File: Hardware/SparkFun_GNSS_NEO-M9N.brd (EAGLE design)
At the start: 64.9 x 38 mm, 74 parts, among them J1 MICROMOD_STANDARD, J4 Bus Selection, U1 U-BLOX_NEO-M9N, U2 3.3V, U3 EEPROM, U4 74HC1G04

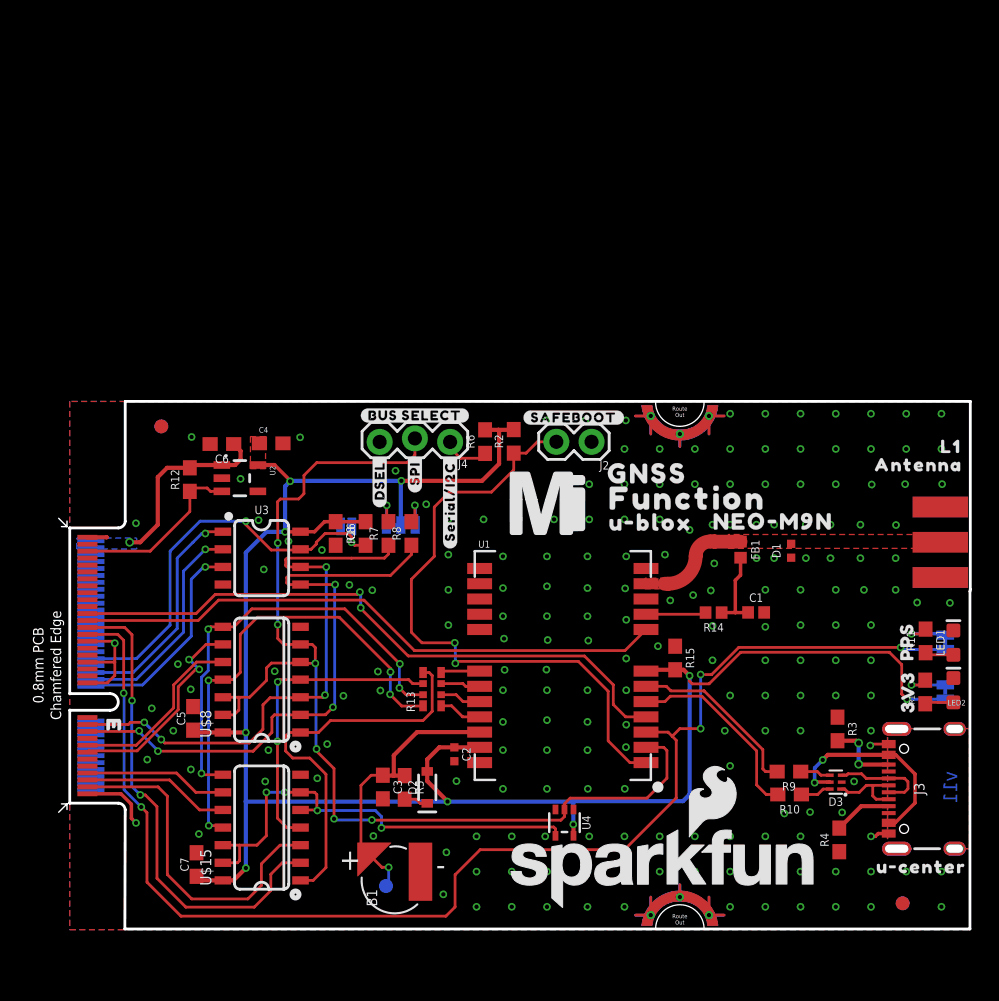
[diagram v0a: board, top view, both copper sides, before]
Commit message: Adds PTH selection silk to bottom
* Chnages MISO/MOSI net label -> PICO/POCI
* Adds text explanation to safeboot pth selection
* Moves some nets around for better ground pour
* Adds a few vias
* Adds measures to LEDs
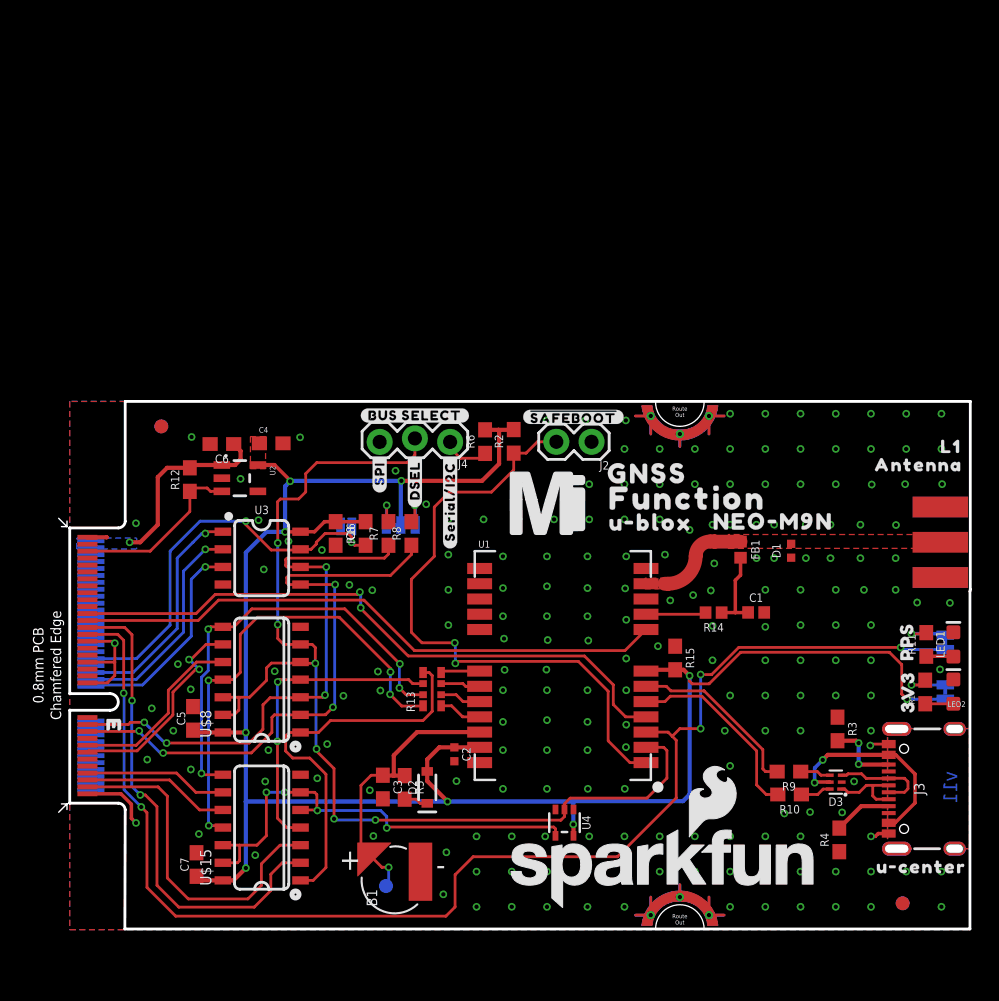
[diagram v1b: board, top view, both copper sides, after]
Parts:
- added U$22: (no value), top:#BUS_SELECT#509
- added U$23: (no value), neom9n:##SAFEBOOT##882188213
- added U$24: (no value), top:#SPI#40313521
- added U$25: (no value), top:#DSEL#40313522
- added U$26: (no value), top:#SERIAL#I2C#40313523
- U$4: device top:#SAFEBOOT#12 -> neom9n:##SAFEBOOT##882188213
- moved U$16 2.54 mm to (22.4, 32.9)
- moved U$19 2.54 mm to (24.9, 32.4)
- moved R11 0.26 mm to (61.8, 20.6)
- moved LED1 0.13 mm to (63.7, 20.6)
- moved LED2 0.10 mm to (63.7, 17.2)
- moved U$4 0.06 mm to (36.3, 37.0)
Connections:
- net RXI/SDI renamed RXI/PICO
- net SDI renamed PICO
- net SDO renamed POCI
- net TXO/SDO renamed TXO/POCI
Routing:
- net GND: vias 201 -> 204

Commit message: Replaces SMA connector with u.FL
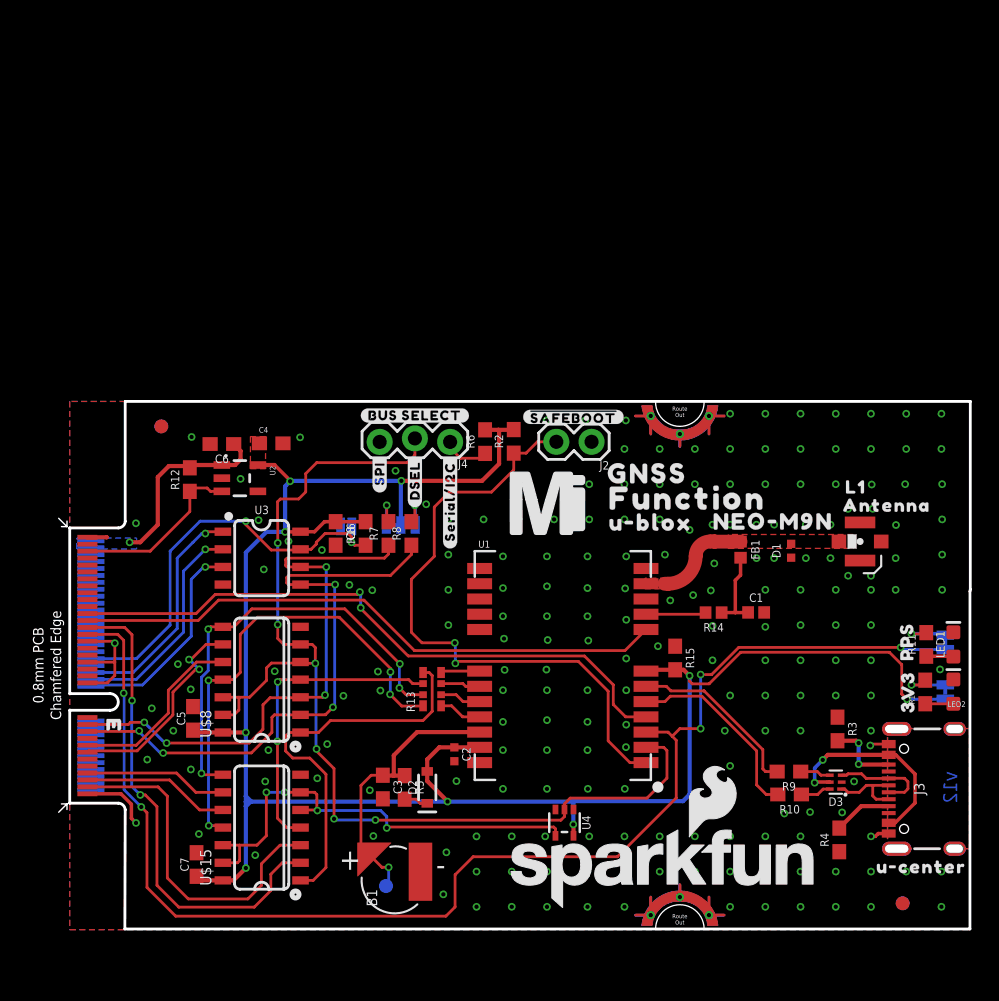
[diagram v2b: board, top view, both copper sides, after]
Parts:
- E1: value ANTENNA-SMA-GROUNDEDEDGE_SMA_THIN -> U.FL; device SparkFun-RF:SMA-EDGE -> SparkFun-Connectors:U.FL
- R5: value 1k -> 3.3k
- R7, R8: value 4.7k -> 2.2k
- moved U$14 7.45 mm to (56.7, 31.9)
- moved E1 5.79 mm to (57.0, 28.0), turned to 180 degrees
- moved U$7 3.71 mm to (58.9, 30.6)
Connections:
- net GND: now also E1.1, E1.2; no longer E1.GND@0, E1.GND@1, E1.GND@2, E1.GND@3
- net GPS_ANT1: now also E1.FEED; no longer E1.SIG
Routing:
- net 3.3V: track 147.1 -> 148.2 mm
- net GND: vias 204 -> 207
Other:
- board text added: "v12"
- board text removed: "v11"

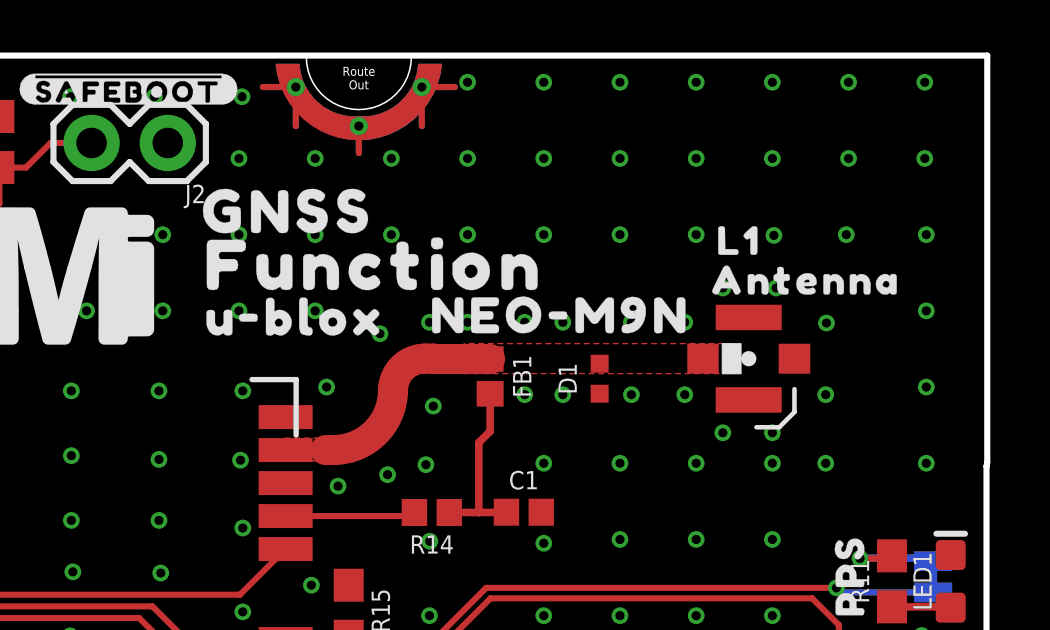
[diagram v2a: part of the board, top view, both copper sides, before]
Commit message: Replaces old ML414H reflowable with new MS421R
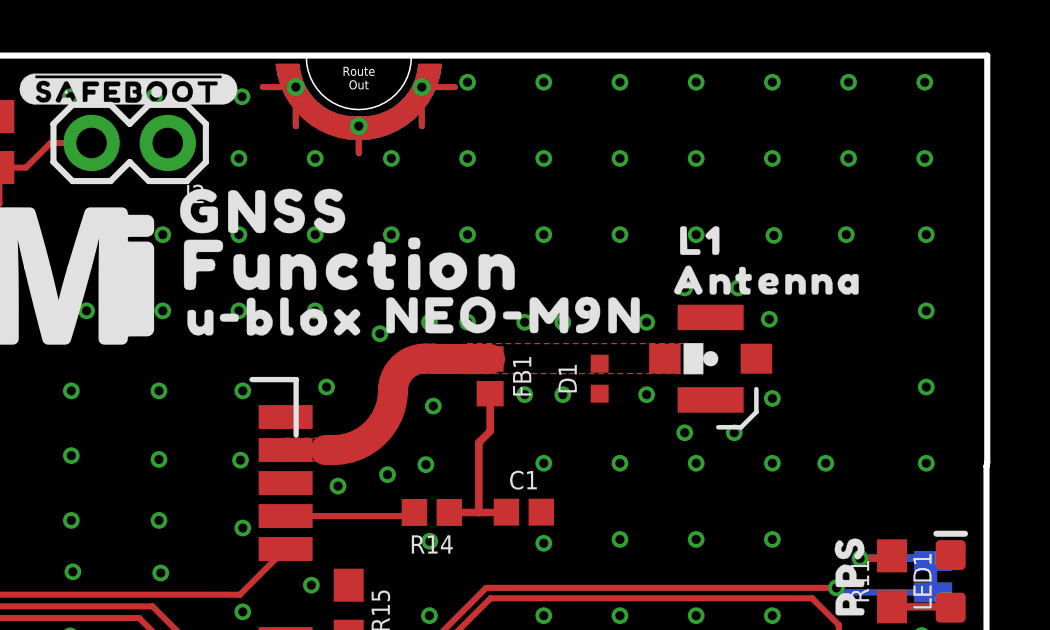
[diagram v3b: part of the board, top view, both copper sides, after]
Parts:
- B1: device SparkFun-Batteries:ML414H_IV01E -> SparkFun-Batteries:MS421R_IV03E
- moved U$6 1.52 mm to (49.2, 29.4)
- moved E1 1.27 mm to (55.7, 28.0)
- moved U$14 1.27 mm to (55.4, 31.9)
- moved U$7 1.27 mm to (57.7, 30.6)
- moved U$21 0.76 mm to (40.9, 32.9)
- moved U$3 0.76 mm to (43.8, 31.1)
- moved U$5 0.63 mm to (41.2, 29.4)
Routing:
- net GND: vias 207 -> 205
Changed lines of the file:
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@@
 <attribute name="VALUE" x="22.7076" y="12.9554" size="0.6096" layer="27" font="vector" ratio="20" rot="R270" align="top-center"/>
 </element>
-<element name="B1" library="SparkFun-Batteries" package="ML414H_IV01E" value="6.8MM_COIN_CELL" x="23.4442" y="3.5814" smashed="yes" rot="R90">
+<element name="B1" library="SparkFun-Batteries" package="MS421R_IV03E" value="6.8MM_COIN_CELL" x="23.4442" y="3.5814" smashed="yes" rot="R90">
 <attribute name="NAME" x="22.174196875" y="1.676396875" size="0.762" layer="25" ratio="15" rot="R90"/>
-<attribute name="PROD_ID" value="BATT-14267" x="23.4442" y="3.5814" size="1.778" layer="27" rot="R90" display="off"/>
+<attribute name="PROD_ID" value="BAT-16685" x="23.4442" y="3.5814" size="1.778" layer="27" rot="R90" display="off"/>
 </element>
 <element name="R7" library="SparkFun-Resistors" package="0603" value="2.2k" x="22.987" y="28.575" smashed="yes" rot="R90">
@@
 <attribute name="VALUE" x="62.5348" y="10.16" size="0.762" layer="27" rot="R90" align="center"/>
 </element>
-<element name="E1" library="SparkFun-Connectors" package="U.FL" value="U.FL" x="56.9976" y="27.9962" smashed="yes" rot="R180">
-<attribute name="PROD_ID" value="CONN-09193" x="56.9976" y="27.9962" size="1.778" layer="27" rot="R180" display="off"/>
-<attribute name="SF_ID" value="WRL-09144" x="56.9976" y="27.9962" size="1.778" layer="27" rot="R180" display="off"/>
-<attribute name="VALUE" value="U.FL" x="56.9976" y="27.9962" size="1.778" layer="27" rot="R180" display="off"/>
+<element name="E1" library="SparkFun-Connectors" package="U.FL" value="U.FL" x="55.7276" y="27.9962" smashed="yes" rot="R180">
+<attribute name="PROD_ID" value="CONN-09193" x="55.7276" y="27.9962" size="1.778" layer="27" rot="R180" display="off"/>
+<attribute name="SF_ID" value="WRL-09144" x="55.7276" y="27.9962" size="1.778" layer="27" rot="R180" display="off"/>
+<attribute name="VALUE" value="U.FL" x="55.7276" y="27.9962" size="1.778" layer="27" rot="R180" display="off"/>
 </element>
 <element name="FB1" library="SparkFun-Coils" package="0402" value="120Ω" x="48.3774" y="27.4064" smashed="yes" rot="R270">
@@
 <element name="U$1" library="top" package="3V313" value="" x="60.452" y="17.145" smashed="yes" rot="R90"/>
 <element name="U$2" library="top" package="PPS13" value="" x="60.3758" y="20.7772" smashed="yes" rot="R90"/>
-<element name="U$5" library="top" package="U#BLOX11" value="" x="41.8846" y="29.3624" smashed="yes"/>
-<element name="U$6" library="top" package="NEO#M9N12" value="" x="50.7238" y="29.4386" smashed="yes"/>
-<element name="U$7" library="top" package="ANTENNA14" value="" x="58.928" y="30.607" smashed="yes"/>
+<element name="U$5" library="top" package="U#BLOX11" value="" x="41.2496" y="29.3624" smashed="yes"/>
+<element name="U$6" library="top" package="NEO#M9N12" value="" x="49.1998" y="29.4386" smashed="yes"/>
+<element name="U$7" library="top" package="ANTENNA14" value="" x="57.658" y="30.607" smashed="yes"/>
 <element name="U$9" library="top" package="U#CENTER15" value="" x="61.41" y="4.538" smashed="yes"/>
 <element name="U$10" library="top" package="#I2C#18" value="" x="23.912" y="27.424" smashed="yes" rot="MR0"/>
@@
 <element name="LOGO2" library="SparkFun-Aesthetics" package="SFE_LOGO_NAME_FLAME_.2" value="SFE_LOGO_NAME_FLAME.2_INCH" x="42.799" y="4.4196" smashed="yes"/>
 <element name="LOGO3" library="SparkFun-Aesthetics" package="OSHW-LOGO-S" value="OSHW-LOGOS" x="10.16" y="2.54" smashed="yes" rot="MR0"/>
-<element name="U$3" library="top" package="FUNCTION521" value="" x="44.5262" y="31.115" smashed="yes"/>
+<element name="U$3" library="top" package="FUNCTION521" value="" x="43.7642" y="31.115" smashed="yes"/>
 <element name="R3" library="SparkFun-Resistors" package="0603" value="5.1k" x="55.372" y="14.478" smashed="yes" rot="R270">
 <attribute name="NAME" x="56.134" y="14.478" size="0.6096" layer="25" font="vector" ratio="20" rot="R270" align="bottom-center"/>
@@
 </element>
 <element name="U$11" library="SparkFun-MicroMod" package="MICROMOD_MI_LOGO_1" value="" x="34.4932" y="30.7848" smashed="yes"/>
-<element name="U$14" library="top" package="L1321542" value="" x="56.6928" y="31.9278" smashed="yes"/>
+<element name="U$14" library="top" package="L1321542" value="" x="55.4228" y="31.9278" smashed="yes"/>
 <element name="U$8" library="SparkFun-IC-Logic" package="SO14" value="74LVC4066D_QUAD_BILATERAL_SWITCH" x="13.843" y="17.399" smashed="yes" rot="R90">
 <attribute name="NAME" x="10.2108" y="13.843" size="0.8128" layer="25" font="vector" ratio="16" rot="R90"/>
@@
 </element>
 <element name="U$20" library="top" package="#WP#13215403132222564" value="" x="19.812" y="27.432" smashed="yes" rot="MR0"/>
-<element name="U$21" library="top" package="GNSS2222502" value="" x="41.656" y="32.893" smashed="yes"/>
+<element name="U$21" library="top" package="GNSS2222502" value="" x="40.894" y="32.893" smashed="yes"/>
 <element name="U$12" library="top" package="#3V3_LED#403132222514" value="" x="59.563" y="17.145" smashed="yes" rot="MR0"/>
 <element name="U$13" library="top" package="#PPS_LED#403132222514" value="" x="59.563" y="20.701" smashed="yes" rot="MR0"/>
@@
 <wire x1="43.2" y1="35.75" x2="41.9" y2="37.05" width="0.2032" layer="1"/>
 <via x="60.2488" y="32.131" extent="1-16" drill="0.3048"/>
-<via x="59.5884" y="29.1846" extent="1-16" drill="0.3048"/>
+<via x="57.6834" y="29.3116" extent="1-16" drill="0.3048"/>
 <contactref element="R3" pad="1"/>
 <contactref element="R4" pad="1"/>
@@
 <via x="52.705" y="24.511" extent="1-16" drill="0.3048"/>
 <via x="55.245" y="24.511" extent="1-16" drill="0.3048"/>
-<via x="54.864" y="29.21" extent="1-16" drill="0.3048"/>
-<via x="53.086" y="29.21" extent="1-16" drill="0.3048"/>
+<via x="53.594" y="29.21" extent="1-16" drill="0.3048"/>
 <via x="44.704" y="28.829" extent="1-16" drill="0.3048"/>
 <via x="46.482" y="26.416" extent="1-16" drill="0.3048"/>
 <via x="43.307" y="23.749" extent="1-16" drill="0.3048"/>
 <via x="44.958" y="24.13" extent="1-16" drill="0.3048"/>
-<via x="57.912" y="30.353" extent="1-16" drill="0.3048"/>
+<via x="56.642" y="30.353" extent="1-16" drill="0.3048"/>
 <via x="57.785" y="24.511" extent="1-16" drill="0.3048"/>
-<via x="59.563" y="26.797" extent="1-16" drill="0.3048"/>
-<via x="57.785" y="25.527" extent="1-16" drill="0.3048"/>
-<via x="54.864" y="26.797" extent="1-16" drill="0.3048"/>
-<via x="53.086" y="26.797" extent="1-16" drill="0.3048"/>
+<via x="57.785" y="26.67" extent="1-16" drill="0.3048"/>
+<via x="56.515" y="25.527" extent="1-16" drill="0.3048"/>
+<via x="53.594" y="26.797" extent="1-16" drill="0.3048"/>
 <via x="50.8" y="29.21" extent="1-16" drill="0.3048"/>
 <via x="50.8" y="26.797" extent="1-16" drill="0.3048"/>
@@
 <via x="62.9158" y="27.051" extent="1-16" drill="0.3048"/>
 <via x="62.9158" y="24.511" extent="1-16" drill="0.3048"/>
-<via x="56.134" y="30.353" extent="1-16" drill="0.3048"/>
-<via x="56.134" y="25.527" extent="1-16" drill="0.3048"/>
+<via x="54.864" y="30.353" extent="1-16" drill="0.3048"/>
+<via x="54.864" y="25.527" extent="1-16" drill="0.3048"/>
 </signal>
 <signal name="SCL/SCK">
@@
 <vertex x="47.5" y="28.5"/>
 <vertex x="47.5" y="27.5"/>
-<vertex x="56.5" y="27.5"/>
-<vertex x="56.5" y="28.5"/>
+<vertex x="54.849" y="27.5"/>
+<vertex x="54.849" y="28.5"/>
 </polygon>
 <wire x1="48.3774" y1="27.9864" x2="46.5136" y2="27.9864" width="1" layer="1"/>
